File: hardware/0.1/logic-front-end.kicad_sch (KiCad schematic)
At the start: 41 parts, among them J501 Probe, U501 SN74LVC245A, U502 SN74LVC245A

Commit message: finalise BOM
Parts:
- D501, D502, D503, D504, D505, D506, D507, D508, D509, D510, D511, D512, D513, D514, D515, D516: value TVS -> DESD5V0U1BL; footprint (none) -> josh-passives-smt:D_X1-DFN1006-2; Digikey (none) -> 31-DESD5V0U1BL-7BCT-ND; LCSC (none) -> C1869323; MPN (none) -> DESD5V0U1BL-7B; Manufacturer (none) -> Diodes Incorporated
- J501: footprint (none) -> josh-connectors:PinSocket_2x16_P1.27mm_Horizontal; LCSC C2881759 -> C2881906; MPN X1321FV-2x16-C43D24 -> (none)
- U501, U502: footprint (none) -> josh-dfn-qfn:Texas_RGY0020A_VQFN-20_2.5x4.5mm_P0.5mm; symbol 74xx:74HC245 -> josh-ic:74LVC245A
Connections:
- net GND: now also U501.21 (GND), U502.21 (GND)
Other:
- note added: "Connector PN is 40 pin, will require trimming"

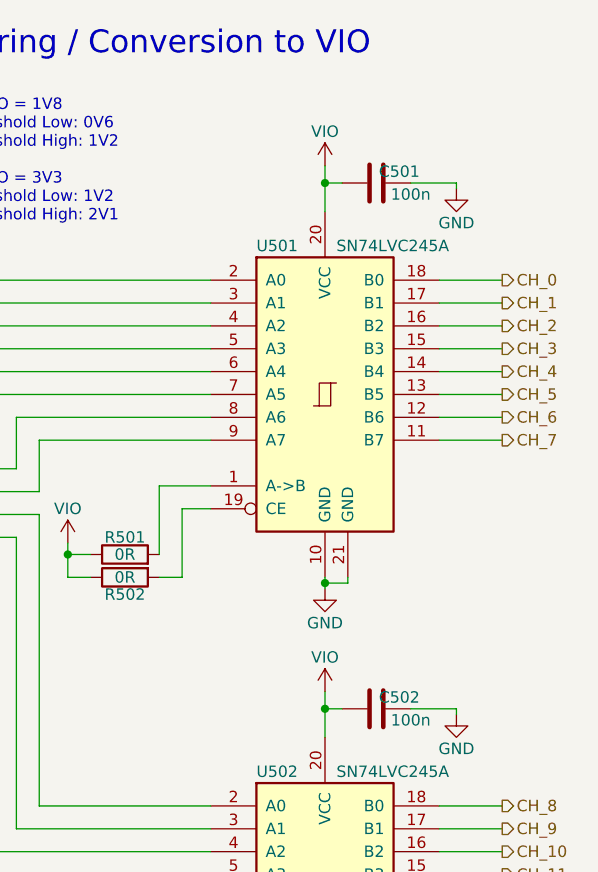
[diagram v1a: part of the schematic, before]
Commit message: all components fit inside outline
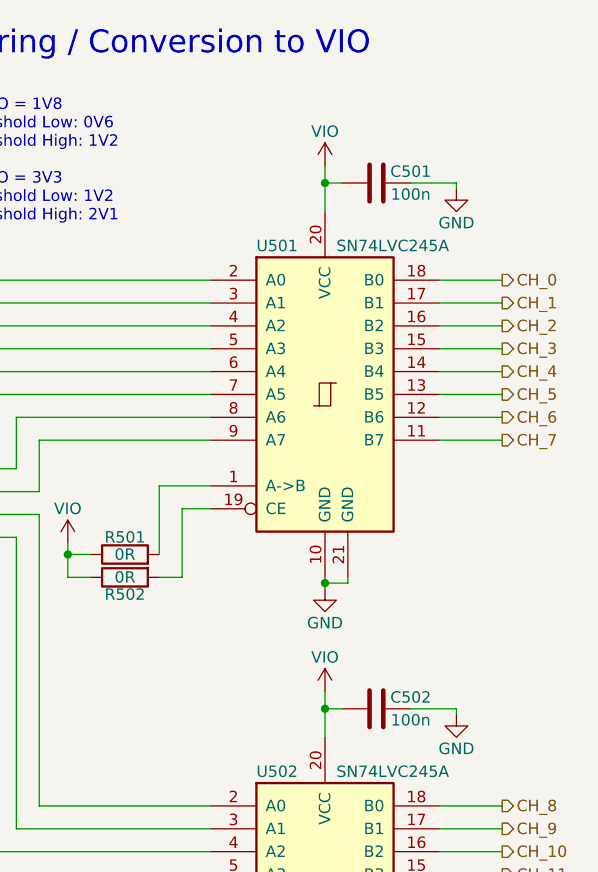
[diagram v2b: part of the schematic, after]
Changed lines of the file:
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@@
   (symbol (lib_id "Device:C") (at 232.41 45.085 90) (unit 1)
     (in_bom yes) (on_board yes)
-    (property "Reference" "C501" (id 0) (at 234.95 43.815 90))
+    (property "Reference" "C501" (id 0) (at 236.22 43.815 90))
     (property "Value" "100n" (id 1) (at 236.22 46.355 90))
     (property "Footprint" "Capacitor_SMD:C_0402_1005Metric" (id 2) (at 236.22 44.1198 0)
@@
   (symbol (lib_id "Device:C") (at 232.41 103.505 90) (unit 1)
     (in_bom yes) (on_board yes)
-    (property "Reference" "C502" (id 0) (at 234.95 102.235 90))
+    (property "Reference" "C502" (id 0) (at 236.22 102.235 90))
     (property "Value" "100n" (id 1) (at 236.22 104.775 90))
     (property "Footprint" "Capacitor_SMD:C_0402_1005Metric" (id 2) (at 236.22 102.5398 0)

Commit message: erc = drc = 0, fixup BOM
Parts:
- J501: MPN (none) -> X1321FR-2x20-C43D24
- R501, R502, R511, R516: MPN RC0402FR-070RL -> C106231; Manufacturer Yageo -> C106231
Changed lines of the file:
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@@
       (effects (font (size 1.27 1.27)) hide)
     )
-    (property "MPN" "RC0402FR-070RL" (id 5) (at 204.47 147.32 0)
-      (effects (font (size 1.27 1.27)) hide)
-    )
-    (property "Manufacturer" "Yageo" (id 6) (at 204.47 147.32 0)
+    (property "MPN" "C106231" (id 5) (at 204.47 147.32 0)
+      (effects (font (size 1.27 1.27)) hide)
+    )
+    (property "Manufacturer" "C106231" (id 6) (at 204.47 147.32 0)
       (effects (font (size 1.27 1.27)) hide)
     )
@@
       (effects (font (size 1.27 1.27)) hide)
     )
-    (property "MPN" " " (id 5) (at 48.26 79.375 0)
+    (property "MPN" "X1321FR-2x20-C43D24" (id 5) (at 48.26 79.375 0)
       (effects (font (size 1.27 1.27)) hide)
     )
@@
       (effects (font (size 1.27 1.27)) hide)
     )
-    (property "MPN" "RC0402FR-070RL" (id 5) (at 204.47 88.9 0)
-      (effects (font (size 1.27 1.27)) hide)
-    )
-    (property "Manufacturer" "Yageo" (id 6) (at 204.47 88.9 0)
+    (property "MPN" "C106231" (id 5) (at 204.47 88.9 0)
+      (effects (font (size 1.27 1.27)) hide)
+    )
+    (property "Manufacturer" "C106231" (id 6) (at 204.47 88.9 0)
       (effects (font (size 1.27 1.27)) hide)
     )
@@
       (effects (font (size 1.27 1.27)) hide)
     )
-    (property "MPN" "RC0402FR-070RL" (id 5) (at 204.47 144.78 0)
-      (effects (font (size 1.27 1.27)) hide)
-    )
-    (property "Manufacturer" "Yageo" (id 6) (at 204.47 144.78 0)
+    (property "MPN" "C106231" (id 5) (at 204.47 144.78 0)
+      (effects (font (size 1.27 1.27)) hide)
+    )
+    (property "Manufacturer" "C106231" (id 6) (at 204.47 144.78 0)
       (effects (font (size 1.27 1.27)) hide)
     )
@@
       (effects (font (size 1.27 1.27)) hide)
     )
-    (property "MPN" "RC0402FR-070RL" (id 5) (at 204.47 86.36 0)
-      (effects (font (size 1.27 1.27)) hide)
-    )
-    (property "Manufacturer" "Yageo" (id 6) (at 204.47 86.36 0)
-      (effects (font (size 1.27 1.27)) hide)
-    )
+    (property "MPN" "C106231" (id 5) (at 204.47 86.36 0)
+      (effects (font (size 1.27 1.27)) hide)
+    )
+    (property "Manufacturer" "C106231" (id 6) (at 204.47 86.36 0)
+      (effects (font (size 1.27 1.27)) hide)
+    )

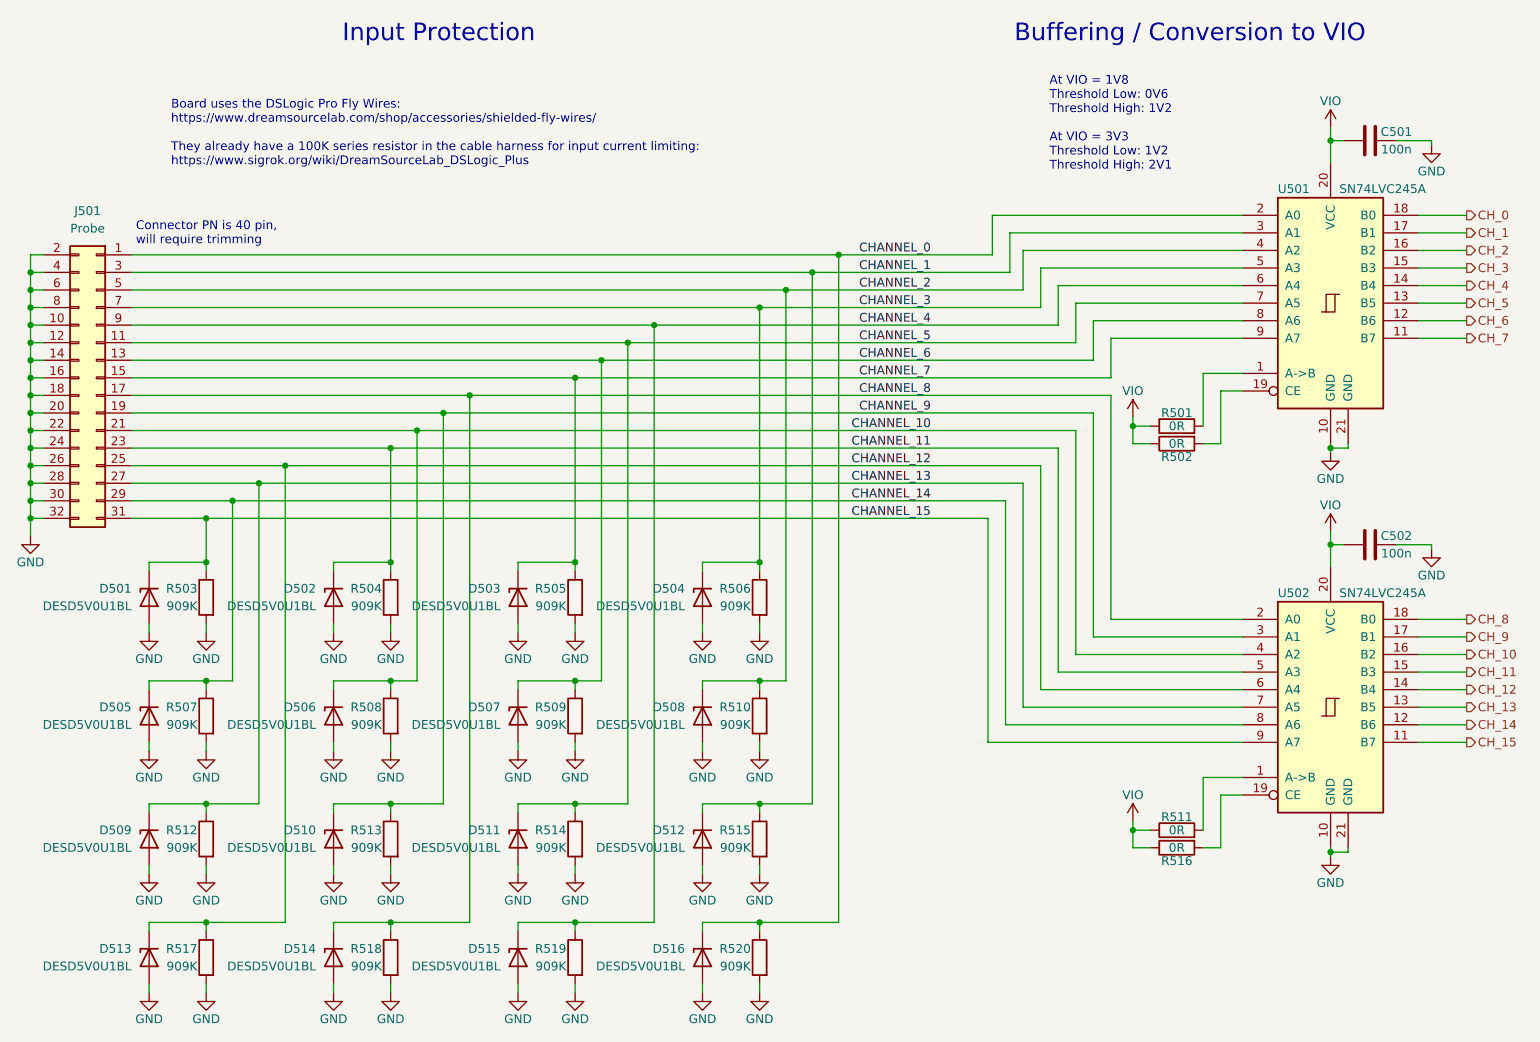
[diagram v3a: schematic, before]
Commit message: component shortage changes
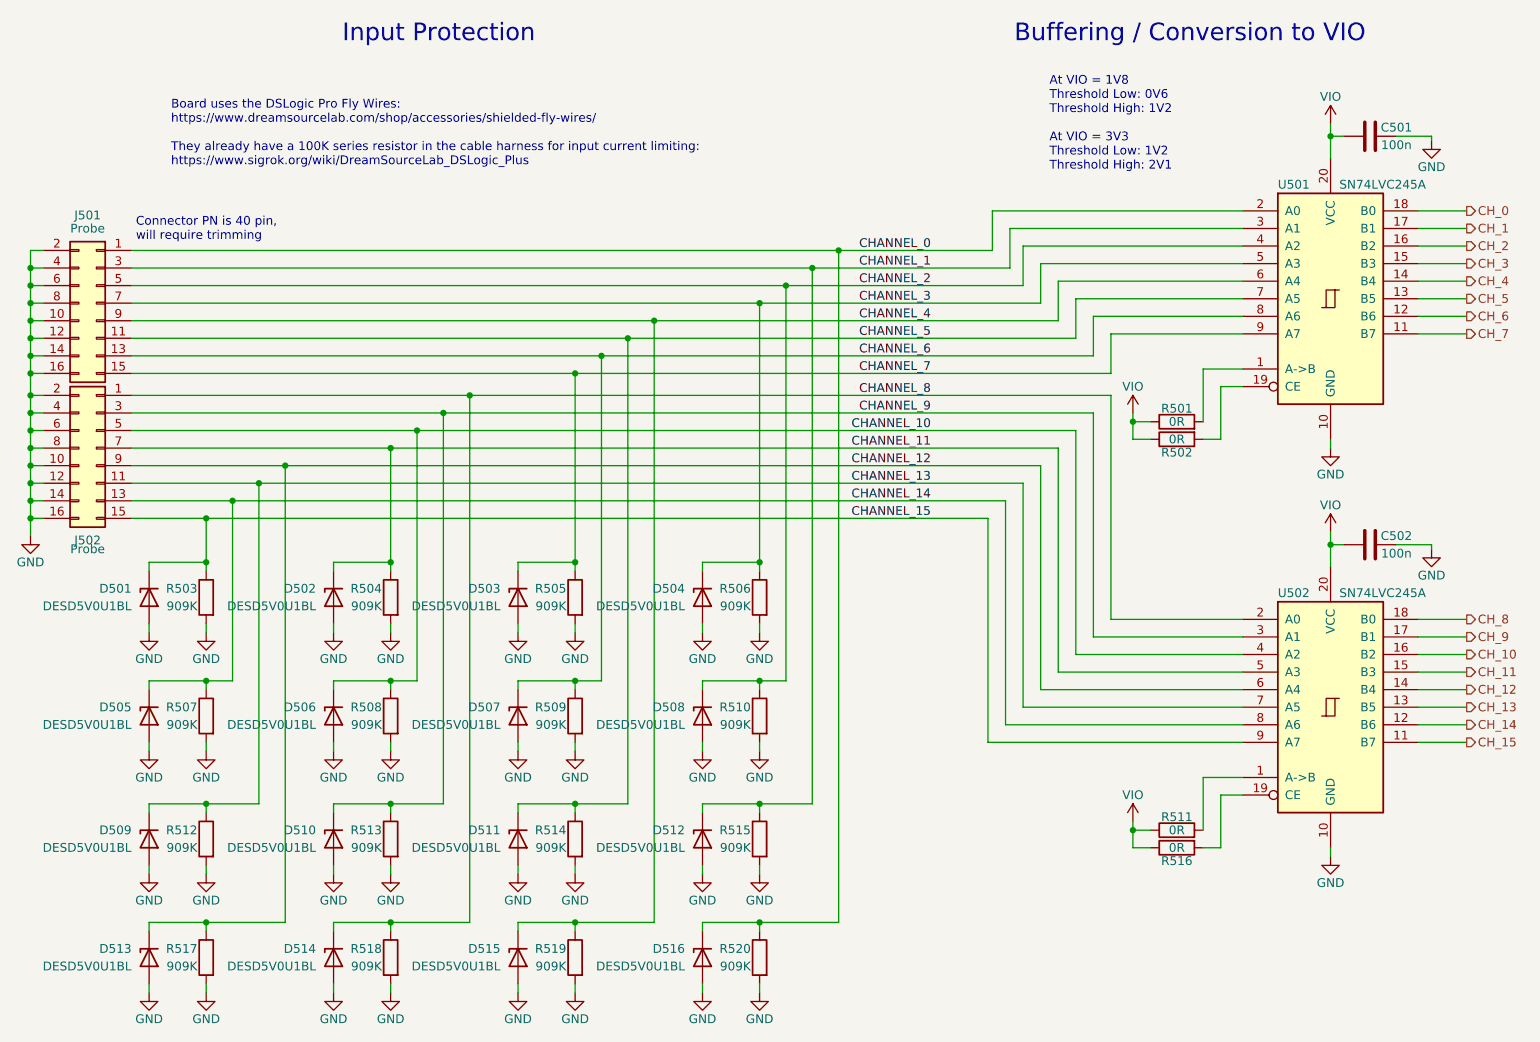
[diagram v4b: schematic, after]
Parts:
- removed J501: Probe, josh-connectors:PinSocket_2x16_P1.27mm_Horizontal, symbol Connector_Generic:Conn_02x16_Odd_Even
- added J501, J502: Probe, josh-connectors:PinSocket_2x08_P1.27mm_Horizontal, symbol Connector_Generic:Conn_02x08_Odd_Even
- R501, R502, R511, R516: MPN C106231 -> RC0402FR-070RL
- U501, U502: footprint josh-dfn-qfn:Texas_RGY0020A_VQFN-20_2.5x4.5mm_P0.5mm -> Package_SO:TSSOP-20_4.4x6.5mm_P0.65mm
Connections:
- net CHANNEL_0: now also J501.1 (Pin_1)
- net CHANNEL_1: now also J501.3 (Pin_3)
- net CHANNEL_10: now also J502.5 (Pin_5)
- net CHANNEL_11: now also J502.7 (Pin_7)
- net CHANNEL_12: now also J502.9 (Pin_9)
- net CHANNEL_13: now also J502.11 (Pin_11)
- net CHANNEL_14: now also J502.13 (Pin_13)
- net CHANNEL_15: now also J502.15 (Pin_15)
- net CHANNEL_2: now also J501.5 (Pin_5)
- net CHANNEL_3: now also J501.7 (Pin_7)
- net CHANNEL_4: now also J501.9 (Pin_9)
- net CHANNEL_5: now also J501.11 (Pin_11)
- net CHANNEL_6: now also J501.13 (Pin_13)
- net CHANNEL_7: now also J501.15 (Pin_15)
- net CHANNEL_8: now also J502.1 (Pin_1)
- net CHANNEL_9: now also J502.3 (Pin_3)
- net GND: now also J501.10 (Pin_10), J501.12 (Pin_12), J501.14 (Pin_14), J501.16 (Pin_16), J501.2 (Pin_2), J501.4 (Pin_4), J501.6 (Pin_6), J501.8 (Pin_8), J502.10 (Pin_10), J502.12 (Pin_12), J502.14 (Pin_14), J502.16 (Pin_16), J502.2 (Pin_2), J502.4 (Pin_4), J502.6 (Pin_6), J502.8 (Pin_8); no longer U501.21 (GND), U502.21 (GND)
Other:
- moved on the sheet: C501, R501, R502
